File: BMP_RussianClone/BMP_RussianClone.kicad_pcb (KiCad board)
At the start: 2 copper layers, 42.1 x 116 mm, 57 parts, among them J1 BARREL_JACK, Q1 MMBT3904, Q2 MMBT3904, Q3 MMBT3904, Q4 MMBT3904

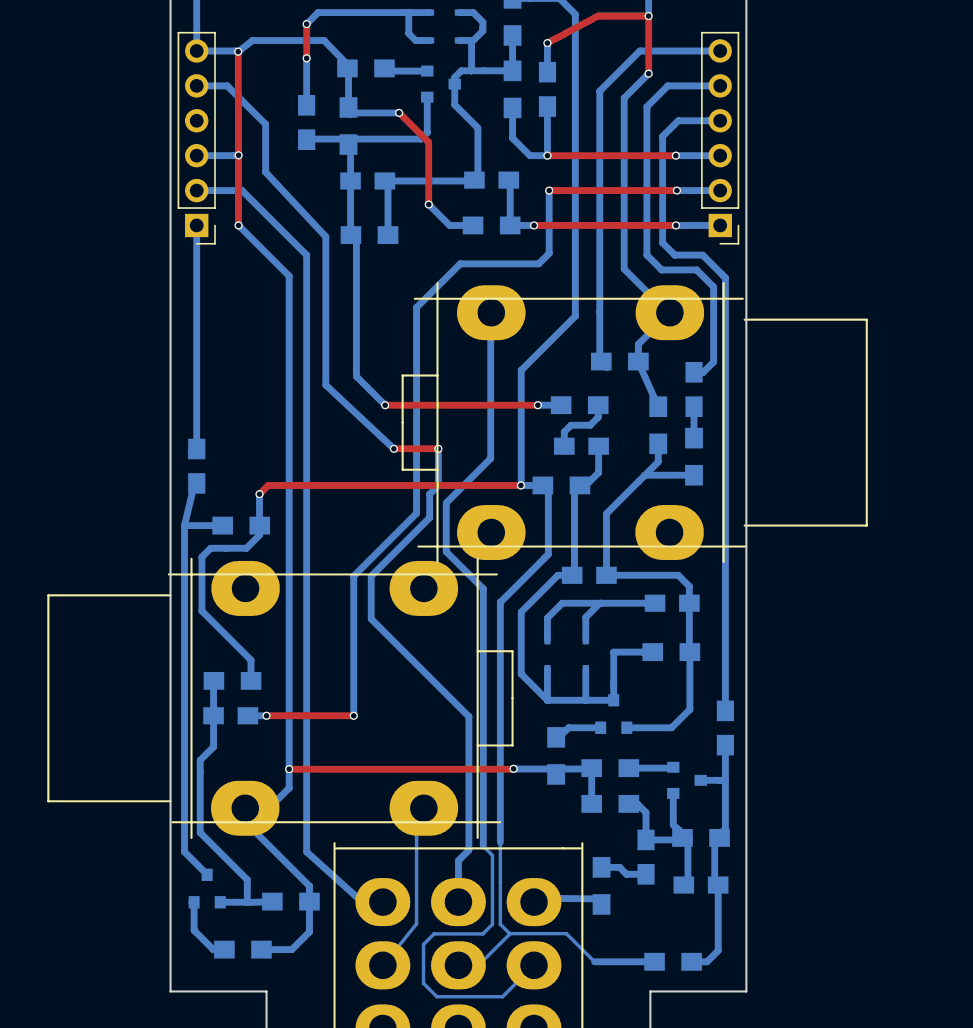
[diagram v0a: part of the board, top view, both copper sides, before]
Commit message: Moved sockets closer to  vertical edges
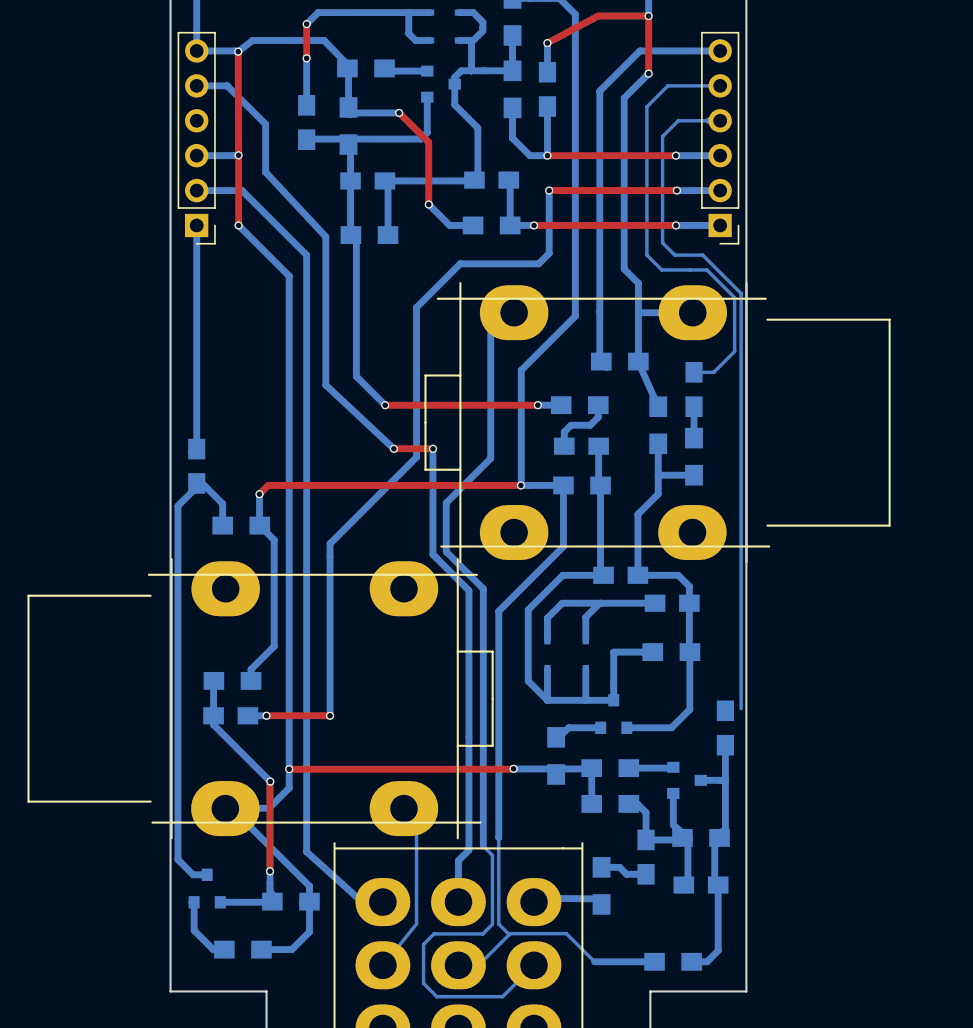
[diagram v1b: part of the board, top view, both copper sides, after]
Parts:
- C10: value 3.9nF -> 4.7nF
- C13, C3: value 100nF -> 1uF
- C2, C6, C9: value 470pF -> 560pF
- C5, C8: value 47nF -> 1uF
- R17: value 20K -> 39K
- R19: value 470K -> 430K
- R22: value 2K7 -> 3K3
- moved C6 2.29 mm to (86.9, 158.6)
- moved J_IN1 1.66 mm to (85.6, 147.4)
- moved R10 1.50 mm to (84.0, 152.0)
- moved J_OUT1 1.45 mm to (64.6, 167.5)
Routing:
- net /LED_AN: track 75.2 -> 70.9 mm
- net Net-(C5-Pad2): track 36.5 -> 32.5 mm
- net /SUS_P2: track 30.1 -> 32.3 mm
- net Net-(C13-Pad1): track 32.5 -> 34.6 mm
- net Net-(C6-Pad1): track 39.2 -> 40.7 mm
- net /+9V: track 137.7 -> 136.2 mm
- net /TONE_P2: track 67.9 -> 66.9 mm
- net /GND: track 245.8 -> 245.2 mm
- net Net-(C12-Pad1): track 22.9 -> 22.7 mm, vias 0 -> 2
